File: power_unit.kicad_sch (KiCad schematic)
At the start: 51 parts, among them J1 ATX-20, U1 LM7805_TO220, U2 LM7905_TO220, X1 Power, X2 Address, X3 Data, X4 Mode, X5 Control, X6 Clock, X7 Power SW, X8 Reset SW, X9 Power LED

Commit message: Add files via upload
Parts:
- added X10: RTC Standby, Connector_PinSocket_2.54mm:PinSocket_1x02_P2.54mm_Vertical, symbol Connector_Generic:Conn_01x02
- J1: footprint Connector_Molex:Molex_Mini-Fit_Jr_5566-20A_2x10_P4.20mm_Vertical -> Connector_Molex:Molex_Mini-Fit_Jr_5566-20A2_2x10_P4.20mm_Vertical
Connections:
- net +5VSB: now also X10.2 (Pin_2)
- net GND: now also X10.1 (Pin_1)
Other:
- moved on the sheet: R8, X9

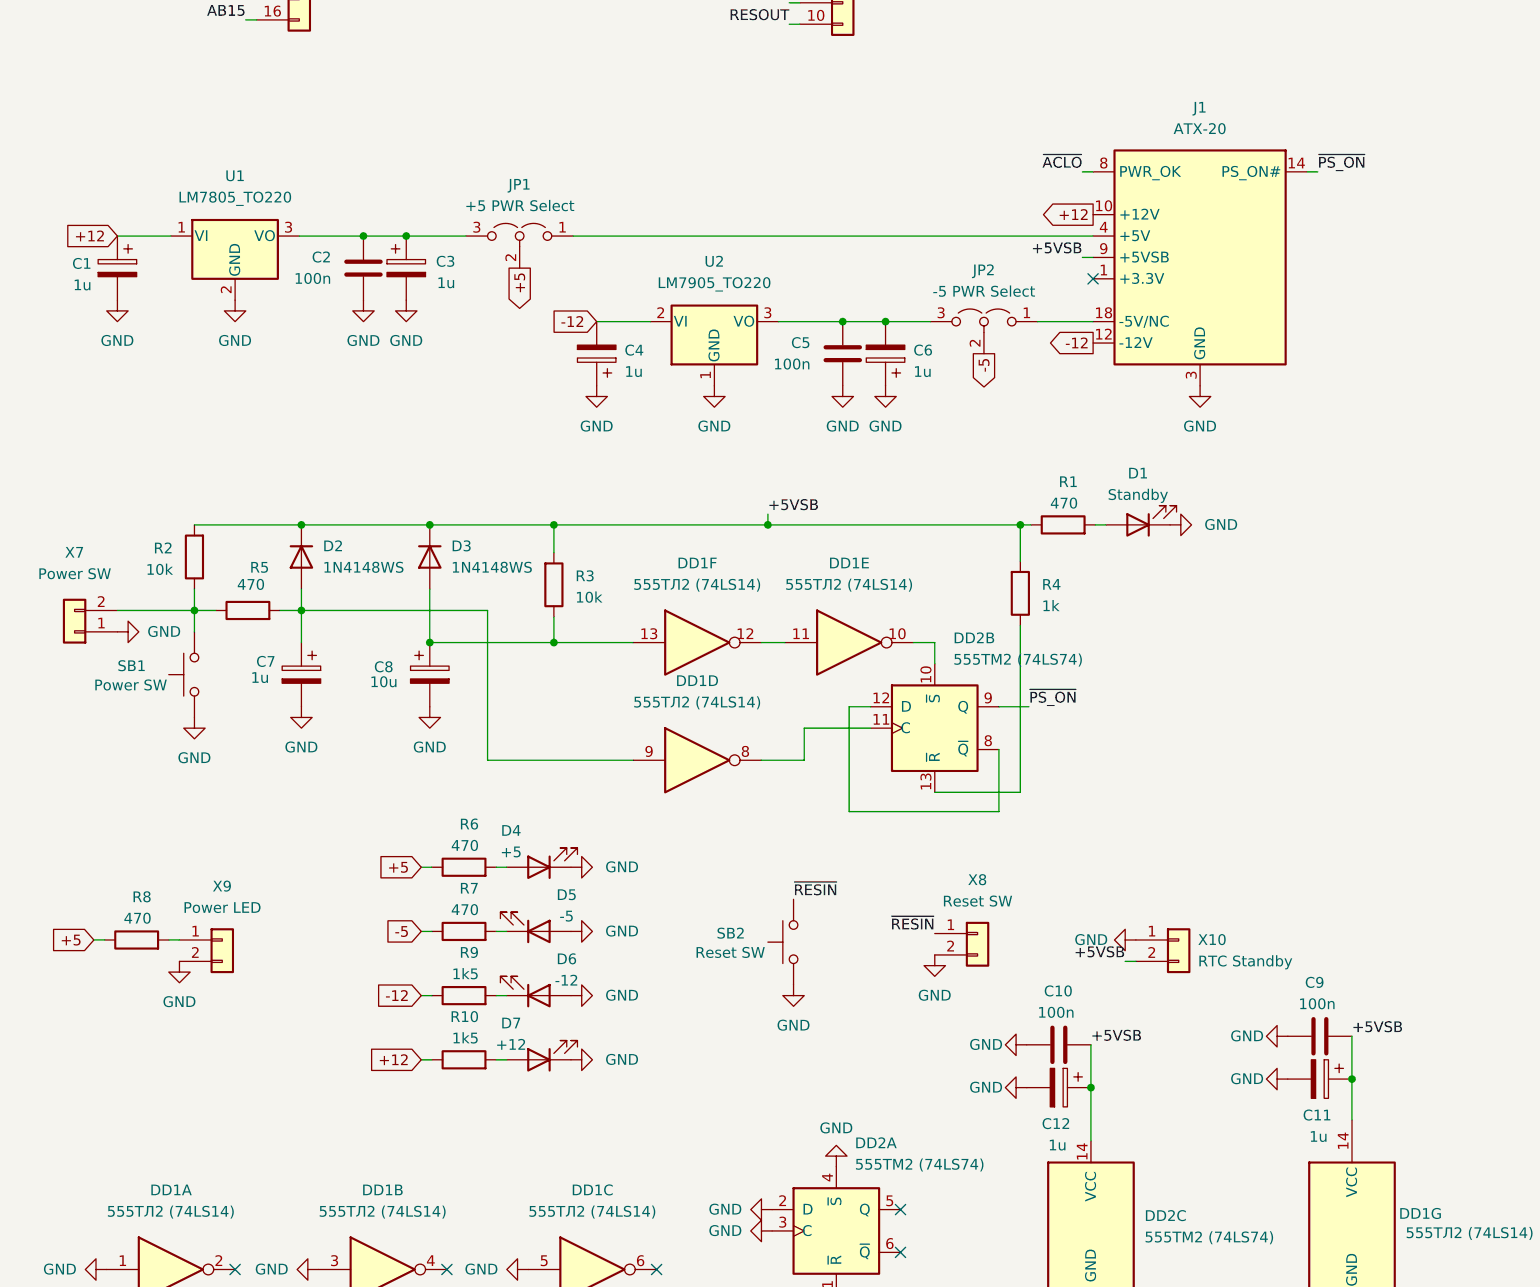
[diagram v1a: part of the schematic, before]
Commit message: Add files via upload
Removed +5V LVR, added connection 'PG_OK' to 'ResIn'.

Удалён линейный стабилизатор +5В, добавлено соединение 'PG_OK' с 'ResIn'.
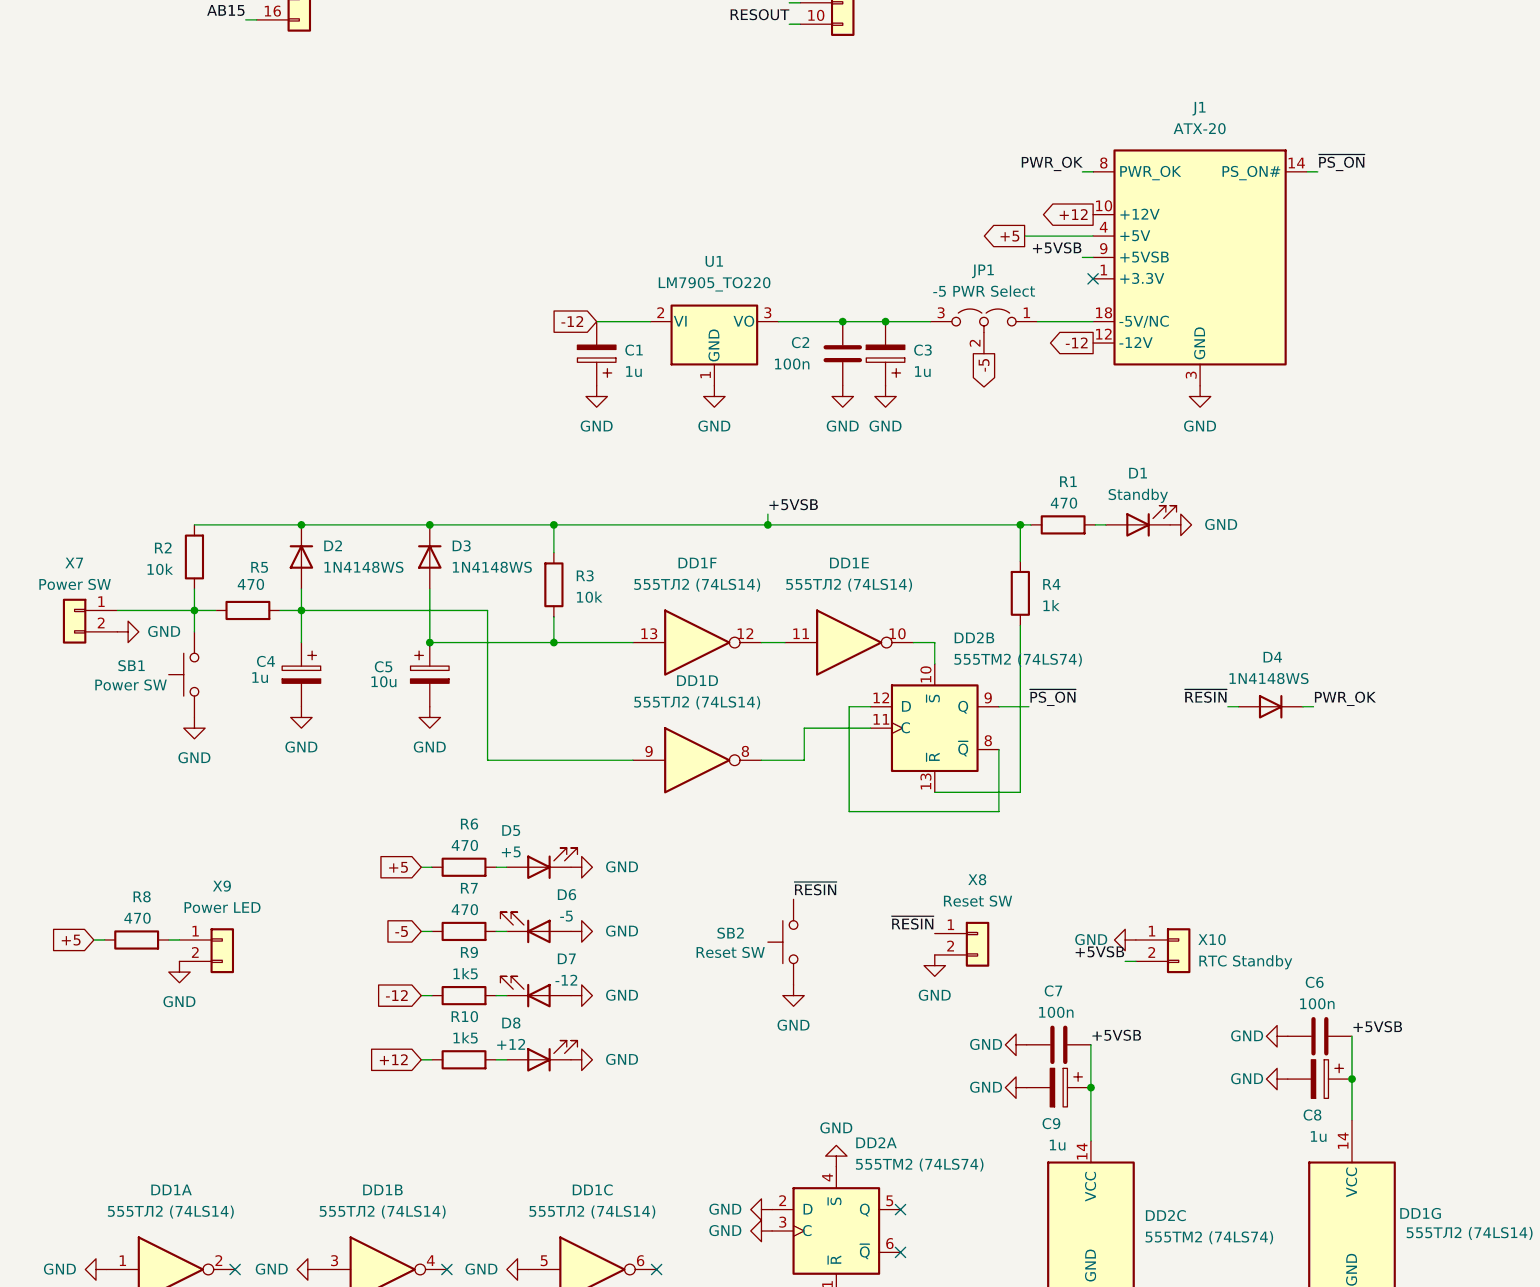
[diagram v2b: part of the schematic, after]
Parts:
- removed C1, C3: 1u, Capacitor_Tantalum_SMD:CP_EIA-3216-18_Kemet-A_Pad1.58x1.35mm_HandSolder, symbol Device:C_Polarized
- removed C2: 100n, Capacitor_SMD:C_0805_2012Metric_Pad1.18x1.45mm_HandSolder, symbol Device:C
- removed JP1: +5 PWR Select, Connector_PinHeader_2.54mm:PinHeader_1x03_P2.54mm_Vertical, symbol Jumper:Jumper_3_Open
- removed U1: LM7805_TO220, Package_TO_SOT_THT:TO-220-3_Horizontal_TabDown, symbol Regulator_Linear:LM7805_TO220
- added D4: 1N4148WS, Diode_SMD:D_SOD-323, symbol Diode:1N4148WS
- renumbered C4 to C1, C5 to C2, C6 to C3, C7 to C4, C8 to C5, C9 to C6, C10 to C7, C11 to C8, C12 to C9, D4 to D5, D5 to D6, D6 to D7, D7 to D8, JP2 to JP1, U2 to U1
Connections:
- net +5: now also J1.19 (+5V), J1.20 (+5V), J1.4 (+5V), J1.6 (+5V)
- net GND: now also X7.2 (Pin_2); no longer X7.1 (Pin_1)
- net ~{RESIN}: now also D4.2 (A)
- net at R2.1, R5.1, SB1.2: now also X7.1 (Pin_1); no longer X7.2 (Pin_2)
- net ~{ACLO} renamed PWR_OK
- net PWR_OK: now also D4.1 (K)
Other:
- moved on the sheet: X7

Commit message: Update
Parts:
- removed H1, H2, H3, H4: MountingHole_Pad, MountingHole:MountingHole_3.2mm_M3_Pad_Via, symbol Mechanical:MountingHole_Pad
- added C4, C6: 100u, Capacitor_Tantalum_SMD:CP_EIA-3528-21_Kemet-B_Pad1.50x2.35mm_HandSolder, symbol Device:C_Polarized
- added C5: 100n, Capacitor_SMD:C_0805_2012Metric_Pad1.18x1.45mm_HandSolder, symbol Device:C
- added C7: 1u, Capacitor_Tantalum_SMD:CP_EIA-3216-18_Kemet-A_Pad1.58x1.35mm_HandSolder, symbol Device:C_Polarized
- added DD3: 1006ВИ1 (LM555), Package_DIP:DIP-8_W7.62mm_Socket_LongPads, symbol Timer:LM555xN
- added R1, R2: 1k, Resistor_SMD:R_0805_2012Metric_Pad1.20x1.40mm_HandSolder, symbol Device:R
- added R3: 470, Resistor_SMD:R_0805_2012Metric_Pad1.20x1.40mm_HandSolder, symbol Device:R
- added R8: 10k, Resistor_SMD:R_0805_2012Metric_Pad1.20x1.40mm_HandSolder, symbol Device:R
- added VD1, VD2: 1N4148WS, Diode_SMD:D_SOD-323_HandSoldering, symbol Diode:1N4148WS
- added VD3: CPU Act, LED_SMD:LED_0805_2012Metric_Pad1.15x1.40mm_HandSolder, symbol Device:LED
- added VT1: MMBT2222A, Package_TO_SOT_SMD:SOT-23_Handsoldering, symbol Transistor_BJT:MMBT2222A
- added X7: Conn_01x10, Connector_PinHeader_2.54mm:PinHeader_1x10_P2.54mm_Vertical, symbol Connector_Generic:Conn_01x10
- J1: footprint Connector_Molex:Molex_Mini-Fit_Jr_5566-20A2_2x10_P4.20mm_Vertical -> Library:ATX-20
- VD4: renamed from D2; footprint Diode_SMD:D_SOD-323 -> Diode_SMD:D_SOD-323_HandSoldering
- VD5: renamed from D3; footprint Diode_SMD:D_SOD-323 -> Diode_SMD:D_SOD-323_HandSoldering
- renumbered C6 to C10, C7 to C11, C8 to C12, C9 to C13, C4 to C8, C5 to C9, U1 to DA1, R6 to R10, R7 to R11, R8 to R12, R9 to R13, R10 to R14, R2 to R4, R3 to R5, R4 to R6, R5 to R7, R1 to R9, D8 to VD10, D4 to VD11, D1 to VD6, D5 to VD7, D6 to VD8, D7 to VD9, X9 to X10, X10 to X11, X7 to X8, X8 to X9
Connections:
- net +5: now also R3.1
- net +5VSB: now also DD2.1 (~{R}), DD2.4 (~{S}), C5.1, C7.1, DD3.8 (VCC), R1.2, VT1.3 (C); no longer R9.1
- net AB7: now also R2.2
- net GND: now also C4.2, C5.2, C6.2, C7.2, DD3.1 (GND), X7.1 (Pin_1), X7.10 (Pin_10); no longer DD1.1, DD1.5, DD2.1 (~{R}), DD2.2 (D), DD2.3 (C), DD2.4 (~{S})
- net ~{PS_ON}: now also DD1.5
- net at DD2.5 (Q): now also VD2.1 (K)
- net at DD2.6 (~{Q}): now also DD2.2 (D)
- net at DD1.2: now also DD3.4 (R)
- net at DD2.12 (D), DD2.8 (~{Q}): now also DD1.1
- net at DD1.6: now also VD1.1 (K)
- net INTE renamed ~{WRQ}
- net Single_BCLK renamed F2TTL
- net Single_OSC_TTL renamed OSC_TTL
- new net: R3.2, VD3.2 (A)
- new net: DD2.3 (C), R2.1
- new net: R9.1, VT1.2 (E)
- new net: C4.1, C6.1, DD3.2 (TR), DD3.6 (THR), R8.1, VT1.1 (B)
- new net: DD3.3 (Q), R8.2
- new net: R1.1, VD1.2 (A), VD2.2 (A), VD3.1 (K)
- new net IRQ0: X7.9 (Pin_9)
- new net IRQ1: X7.8 (Pin_8)
- new net IRQ2: X7.7 (Pin_7)
- new net IRQ3: X7.6 (Pin_6)
- new net IRQ4: X7.5 (Pin_5)
- new net IRQ5: X7.4 (Pin_4)
- new net IRQ6: X7.3 (Pin_3)
- new net IRQ7: X7.2 (Pin_2)
- no-connect marks 6 -> 4
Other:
- moved on the sheet: C1, C10, C11, C12, C13, C2, C3, C8, C9, DA1, DD1A, DD1B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

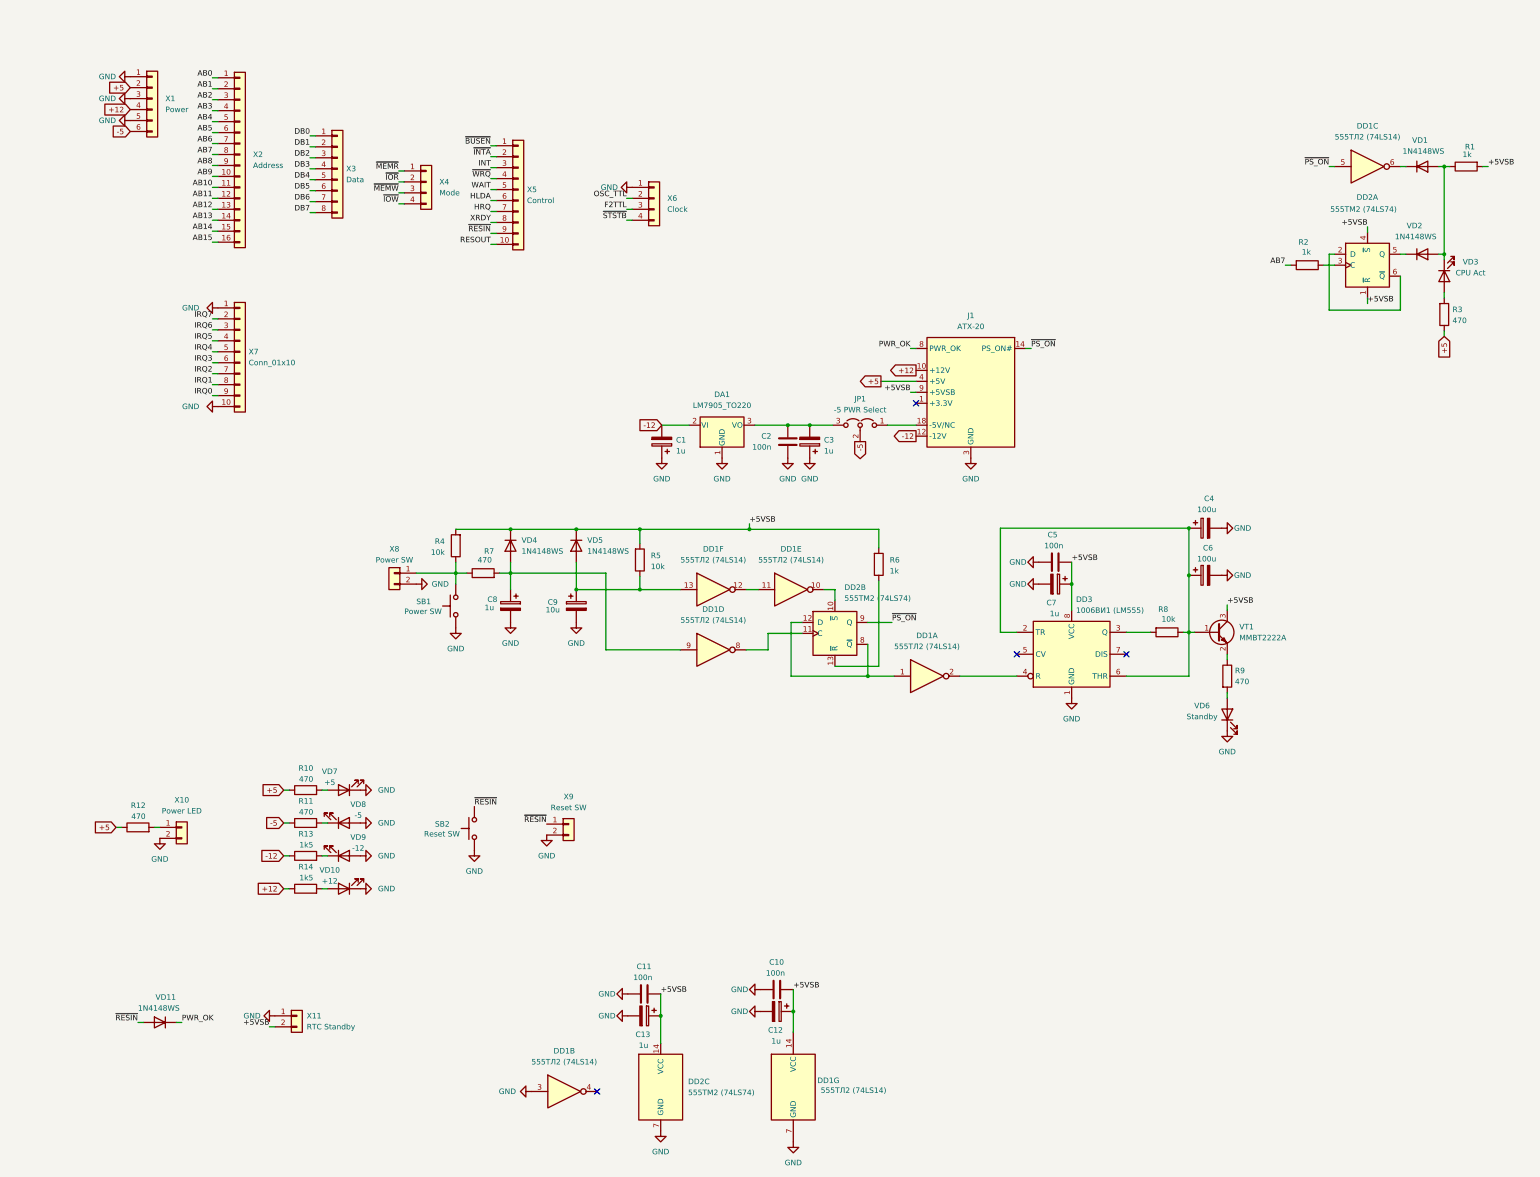
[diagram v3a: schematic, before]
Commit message: Update
Fix footprint's, change optional shematic, add comment's
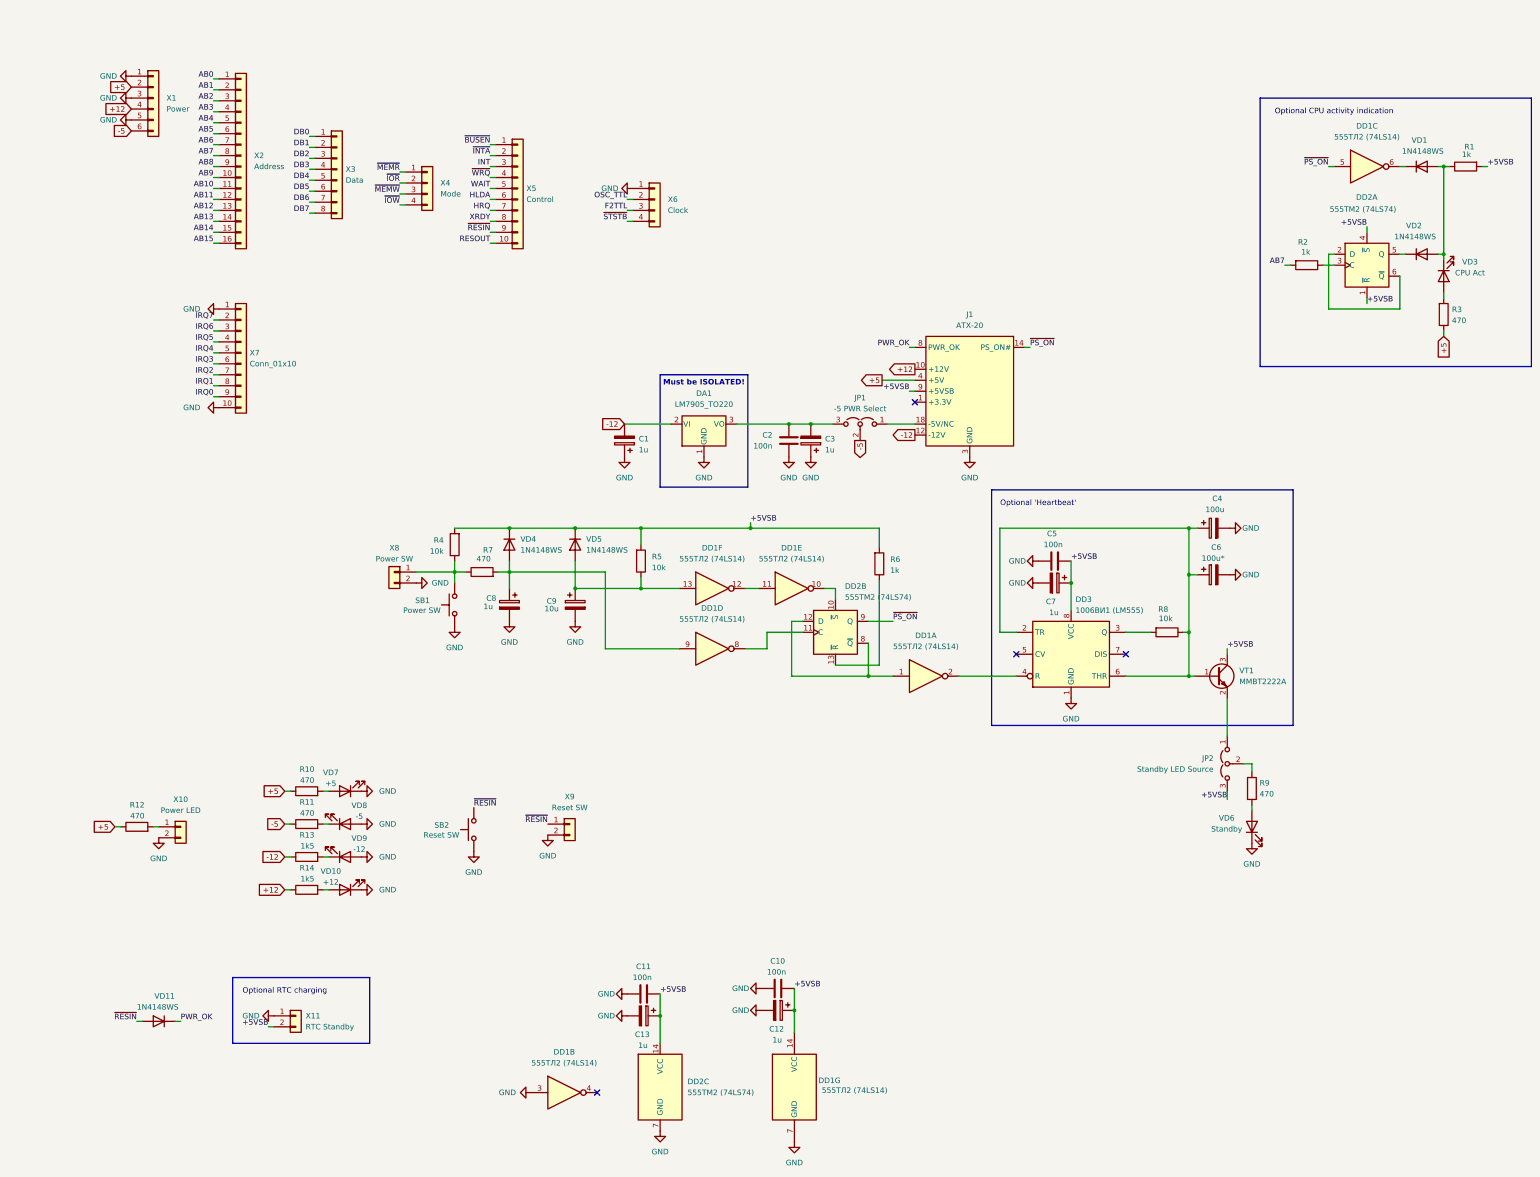
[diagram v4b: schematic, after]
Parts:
- added JP2: Standby LED Source, Jumper:SolderJumper-3_P1.3mm_Open_RoundedPad1.0x1.5mm, symbol Jumper:Jumper_3_Open
- C6: value 100u -> 100u*
- VD11: footprint Diode_SMD:D_SOD-323 -> Diode_SMD:D_SOD-323_HandSoldering
- VT1: footprint Package_TO_SOT_SMD:SOT-23_Handsoldering -> Package_TO_SOT_SMD:SOT-23
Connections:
- net +5VSB: now also JP2.3 (B)
- net at R9.1: now also JP2.2 (C); no longer VT1.2 (E)
- new net: JP2.1 (A), VT1.2 (E)
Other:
- note added: "Must be ISOLATED!"
- note added: "Optional 'Heartbeat'"
- note added: "Optional CPU activity indication"
- note added: "Optional RTC charging"
- moved on the sheet: C1, C4, C6, DA1, R9, VD6, VT1
